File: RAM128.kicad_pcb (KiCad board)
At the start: 4 copper layers, 74.2 x 42.7 mm, 52 parts, among them J1 AppleIIBus, SW1 DMA/ROM, U1 621024, U10 74AHCT32PW, U11 74LVC1G126GW, U12 74AHCT1G04GW, U13 74AHCT1G04GW, U14 74AHCT1G04GW, U15 74AHCT1G04GW, U16 74AHCT1G04GW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

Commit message: 1.2 RC2
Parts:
- added C17: 2u2, stdpads:C_0603, F.Cu at (100.9, 127.8)
- added C18: 2u2, stdpads:C_0603, F.Cu at (98.5, 112.0)
- added R6: DNP, stdpads:R_0805, F.Cu at (95.8, 126.2)
- added U18: 74AHCT1G32GW, stdpads:SOT-353, F.Cu at (103.0, 127.8)
- added U5: 74AHCT1G32GW, stdpads:SOT-353, F.Cu at (106.0, 127.8)
- R5: value 33 -> 0
- U11: value 74LVC1G126GW -> 74AHCT1G126GW
- moved R2 0.10 mm to (101.5, 115.5)
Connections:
- U1 pad 24: GND -> /~{R}W
- U1 pad 29: /R~{W} -> /R~{WE}
- U2 pad 19: /Q3 -> /D~{OE}
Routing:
- net /D~{OE}: track 0.00 -> 41.3 mm, vias 0 -> 6
- net /R~{WE}: track 0.00 -> 34.8 mm, vias 0 -> 2
- net /Q3: track 44.7 -> 10.5 mm, vias 5 -> 1
- net /R~{W}: track 77.5 -> 54.3 mm
- net /~{R}W: track 38.0 -> 58.3 mm, vias 0 -> 2
- net +5V: track 90.2 -> 99.1 mm, vias 75 -> 83
- net /PHI1: track 0.00 -> 7.11 mm, vias 0 -> 1
- net GND: track 79.7 -> 83.6 mm, vias 197 -> 204
- net /PHI0: track 29.2 -> 32.4 mm
- net /R~{CS}: track 108.0 -> 106.4 mm
- net Net-(R2-Pad1): track 39.9 -> 41.5 mm
- net /DMAin: track 118.0 -> 119.3 mm
- net Net-(U10-Pad2): track 25.7 -> 26.2 mm

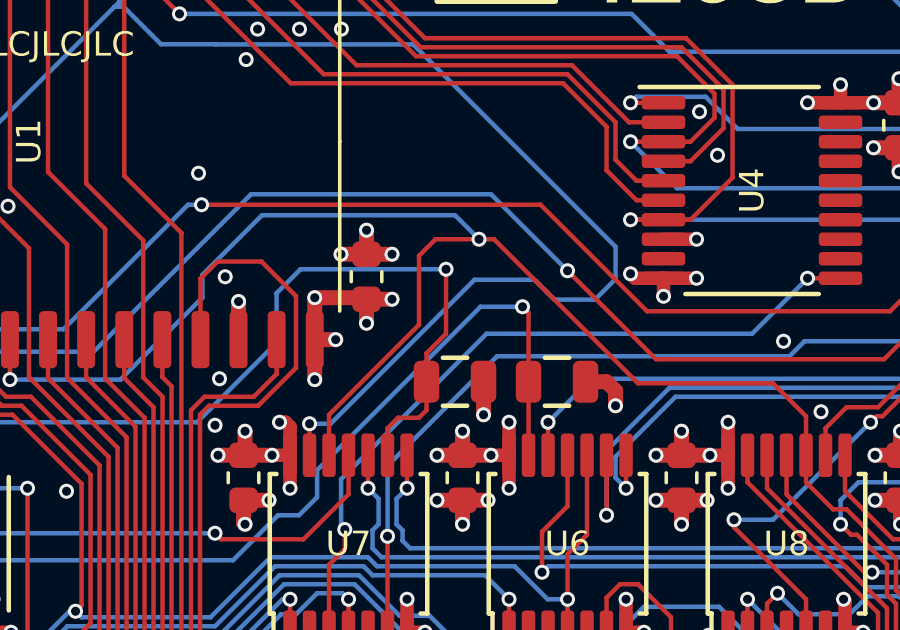
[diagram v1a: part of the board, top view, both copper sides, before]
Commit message: 1.2 RC3
Moved 621024 bypass cap over--that's it
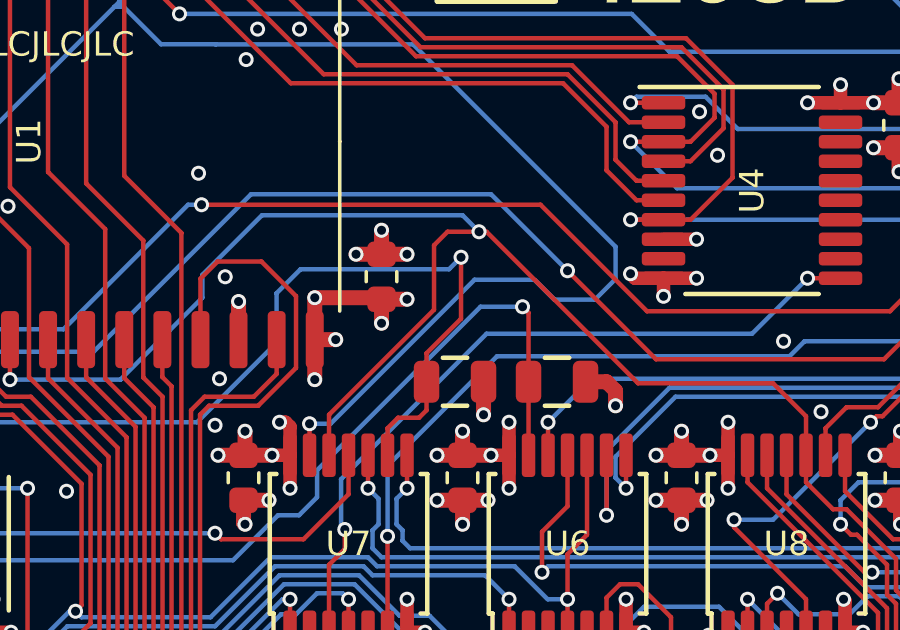
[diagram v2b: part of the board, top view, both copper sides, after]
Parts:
- moved C18 0.50 mm to (99.0, 112.0)
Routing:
- net Net-(R2-Pad1): track 41.5 -> 42.7 mm
- net +5V: track 99.1 -> 99.6 mm

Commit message: 1.2 RC4
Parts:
- R1: value 3k3 -> 22k
- R3: value 10k -> 22k
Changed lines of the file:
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@@
     (at 133.2 123.5 180)
     (tags "resistor")
-    (property "LCSC Part" "C26010")
+    (property "LCSC Part" "C17560")
     (property "Sheetfile" "RAM128.kicad_sch")
     (property "Sheetname" "")
@@
         (effects (font (size 0.254 0.254) (thickness 0.0635)))
     )
-    (fp_text value "3k3" (at 0 0.35) (layer "F.Fab")
+    (fp_text value "22k" (at 0 0.35) (layer "F.Fab")
         (effects (font (size 0.254 0.254) (thickness 0.0635)))
     )
@@
     (at 133.2 125.7 180)
     (tags "resistor")
-    (property "LCSC Part" "C17414")
+    (property "LCSC Part" "C17560")
     (property "Sheetfile" "RAM128.kicad_sch")
     (property "Sheetname" "")
@@
         (effects (font (size 0.254 0.254) (thickness 0.0635)))
     )
-    (fp_text value "10k" (at 0 0.35) (layer "F.Fab")
-        (effects (font (size 0.254 0.254) (thickness 0.0635)))
-    )
+    (fp_text value "22k" (at 0 0.35) (layer "F.Fab")
+        (effects (font (size 0.254 0.254) (thickness 0.0635)))
+    )
